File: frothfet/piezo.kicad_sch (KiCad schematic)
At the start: 3 parts, among them Q19 AO3400A

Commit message: piezo resistor
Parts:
- added R102: 100k, Resistor_SMD:R_0603_1608Metric, symbol Device:R_Small_US
- R90: value 1k -> 100R
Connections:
- net GNDD: now also R102.2
- net at Q19.1 (G), R90.1: now also R102.1
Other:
- moved on the sheet: R90
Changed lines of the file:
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@@
 		)
+	)
+	(junction
+		(at 134.62 109.22)
+		(diameter 0)
+		(color 0 0 0 0)
+	)
+	(junction
+		(at 124.46 100.33)
+		(diameter 0)
+		(color 0 0 0 0)
 	)
 	(wire
@@
 	(wire
 		(pts
-			(xy 123.19 100.33) (xy 127 100.33)
-		)
-		(stroke
-			(width 0)
-			(type default)
-		)
-	)
-	(wire
-		(pts
-			(xy 114.3 100.33) (xy 118.11 100.33)
+			(xy 134.62 109.22) (xy 124.46 109.22)
+		)
+		(stroke
+			(width 0)
+			(type default)
+		)
+	)
+	(wire
+		(pts
+			(xy 121.92 100.33) (xy 124.46 100.33)
+		)
+		(stroke
+			(width 0)
+			(type default)
+		)
+	)
+	(wire
+		(pts
+			(xy 124.46 109.22) (xy 124.46 107.95)
+		)
+		(stroke
+			(width 0)
+			(type default)
+		)
+	)
+	(wire
+		(pts
+			(xy 113.03 100.33) (xy 116.84 100.33)
+		)
+		(stroke
+			(width 0)
+			(type default)
+		)
+	)
+	(wire
+		(pts
+			(xy 124.46 100.33) (xy 127 100.33)
 		)
 		(stroke
@@
 		(pts
 			(xy 134.62 72.39) (xy 134.62 82.55)
+		)
+		(stroke
+			(width 0)
+			(type default)
+		)
+	)
+	(wire
+		(pts
+			(xy 124.46 100.33) (xy 124.46 102.87)
 		)
 		(stroke
@@
 	(hierarchical_label "PIEZO"
 		(shape input)
-		(at 114.3 100.33 180)
+		(at 113.03 100.33 180)
 		(effects
 			(font
@@
 	(symbol
 		(lib_id "Device:R_Small_US")
-		(at 120.65 100.33 270)
+		(at 124.46 105.41 0)
+		(unit 1)
+		(exclude_from_sim no)
+		(in_bom yes)
+		(on_board yes)
+		(dnp no)
+		(fields_autoplaced yes)
+		(property "Reference" "R102"
+			(at 127 104.1399 0)
+			(effects
+				(font
+					(size 1.27 1.27)
+				)
+				(justify left)
+			)
+		)
+		(property "Value" "100k"
+			(at 127 106.6799 0)
+			(effects
+				(font
+					(size 1.27 1.27)
+				)
+				(justify left)
+			)
+		)
+		(property "Footprint" "Resistor_SMD:R_0603_1608Metric"
+			(at 124.46 105.41 0)
+			(effects
+				(font
+					(size 1.27 1.27)
+				)
+				(hide yes)
+			)
+		)
+		(property "Datasheet" "~"
+			(at 124.46 105.41 0)
+			(effects
+				(font
+					(size 1.27 1.27)
+				)
+				(hide yes)
+			)
+		)
+		(property "Description" ""
+			(at 124.46 105.41 0)
+			(effects
+				(font
+					(size 1.27 1.27)
+				)
+				(hide yes)
+			)
+		)
+		(pin "1"
+		)
+		(pin "2"
+		)
+		(instances
+			(project "frothfet"
+				(path "/c83c6236-96e9-46ad-9d7a-9e2efa4a7966/13bd1484-e1d0-414c-b70b-256f3904dbbc"
+					(reference "R102")
+					(unit 1)
+				)
+			)
+		)
+	)
+	(symbol
+		(lib_id "Device:R_Small_US")
+		(at 119.38 100.33 270)
 		(unit 1)
 		(exclude_from_sim no)
@@
 		(fields_autoplaced yes)
 		(property "Reference" "R90"
-			(at 120.65 93.98 90)
-			(effects
-				(font
-					(size 1.27 1.27)
-				)
-			)
-		)
-		(property "Value" "1k"
-			(at 120.65 96.52 90)
+			(at 119.38 93.98 90)
+			(effects
+				(font
+					(size 1.27 1.27)
+				)
+			)
+		)
+		(property "Value" "100R"
+			(at 119.38 96.52 90)
 			(effects
 				(font
@@
 		)
 		(property "Footprint" "Resistor_SMD:R_0603_1608Metric"
-			(at 120.65 100.33 0)
+			(at 119.38 100.33 0)
 			(effects
 				(font
@@
 		)
 		(property "Datasheet" "~"
-			(at 120.65 100.33 0)
+			(at 119.38 100.33 0)
 			(effects
 				(font
@@
 		)
 		(property "Description" ""
-			(at 120.65 100.33 0)
-			(effects
-				(font
-					(size 1.27 1.27)
-				)
-				(hide yes)
-			)
-		)
-		(property "LCSC" ""
-			(at 120.65 100.33 0)
-			(effects
-				(font
-					(size 1.27 1.27)
-				)
-				(hide yes)
-			)
-		)
-		(property "ALT" ""
-			(at 120.65 100.33 0)
-			(effects
-				(font
+			(at 119.38 100.33 0)
+			(effects
+				(font

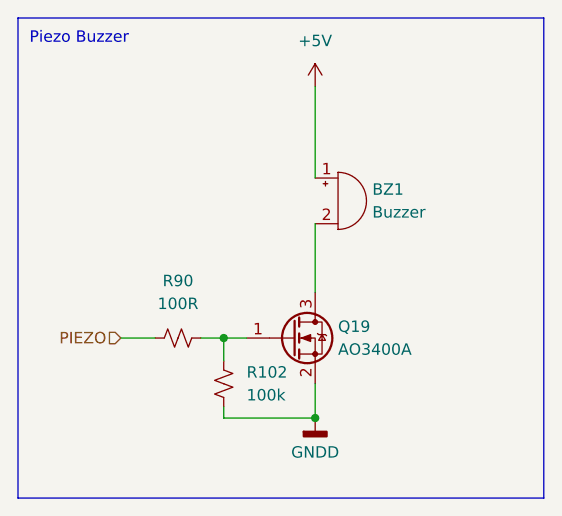
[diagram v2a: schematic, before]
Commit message: silkscreen done, erc+drc passing
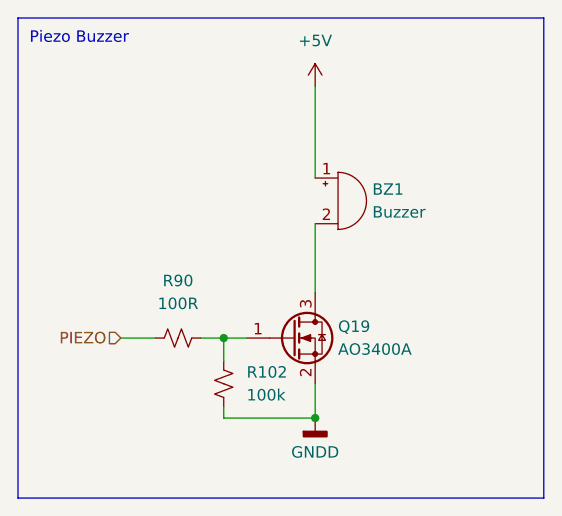
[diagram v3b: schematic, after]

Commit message: bom and placement all check out.  ready for production!
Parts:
- BZ1: Rotation Offset (none) -> 90
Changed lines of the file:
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@@
+			)
+		)
+		(property "Rotation Offset" "90"
+			(at 137.16 85.09 0)
+			(effects
+				(font
+					(size 1.27 1.27)
+				)
+				(hide yes)
 			)
 		)

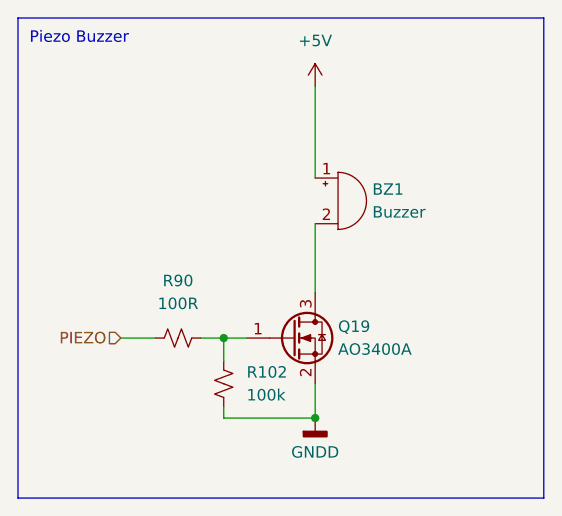
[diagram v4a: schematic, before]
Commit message: pulled in updated esp32-s3 schematic
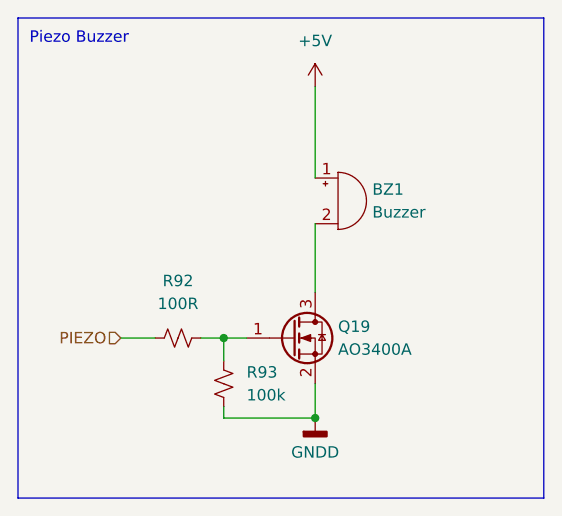
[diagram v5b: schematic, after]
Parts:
- renumbered R90 to R92, R102 to R93
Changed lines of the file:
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@@
 		(dnp no)
 		(fields_autoplaced yes)
-		(property "Reference" "R102"
+		(property "Reference" "R93"
 			(at 127 104.1399 0)
 			(effects
@@
 			(project "frothfet"
 				(path "/c83c6236-96e9-46ad-9d7a-9e2efa4a7966/13bd1484-e1d0-414c-b70b-256f3904dbbc"
-					(reference "R102")
+					(reference "R93")
 					(unit 1)
 				)
@@
 		(dnp no)
 		(fields_autoplaced yes)
-		(property "Reference" "R90"
+		(property "Reference" "R92"
 			(at 119.38 93.98 90)
 			(effects
@@
 			(project "frothfet"
 				(path "/c83c6236-96e9-46ad-9d7a-9e2efa4a7966/13bd1484-e1d0-414c-b70b-256f3904dbbc"
-					(reference "R90")
+					(reference "R92")
 					(unit 1)
 				)
@@
 		(dnp no)
 		(fields_autoplaced yes)
-		(property "Reference" "#PWR0122"
+		(property "Reference" "#PWR0119"
 			(at 134.62 76.2 0)
 			(effects
@@
 			(project "frothfet"
 				(path "/c83c6236-96e9-46ad-9d7a-9e2efa4a7966/13bd1484-e1d0-414c-b70b-256f3904dbbc"
-					(reference "#PWR0122")
+					(reference "#PWR0119")
 					(unit 1)
 				)
@@
 		(dnp no)
 		(fields_autoplaced yes)
-		(property "Reference" "#PWR0123"
+		(property "Reference" "#PWR0120"
 			(at 134.62 115.57 0)
 			(effects
@@
 			(project "frothfet"
 				(path "/c83c6236-96e9-46ad-9d7a-9e2efa4a7966/13bd1484-e1d0-414c-b70b-256f3904dbbc"
-					(reference "#PWR0123")
-					(unit 1)
-				)
+					(reference "#PWR0120")
+					(unit 1)
+				)

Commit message: wired the i2c addresses.
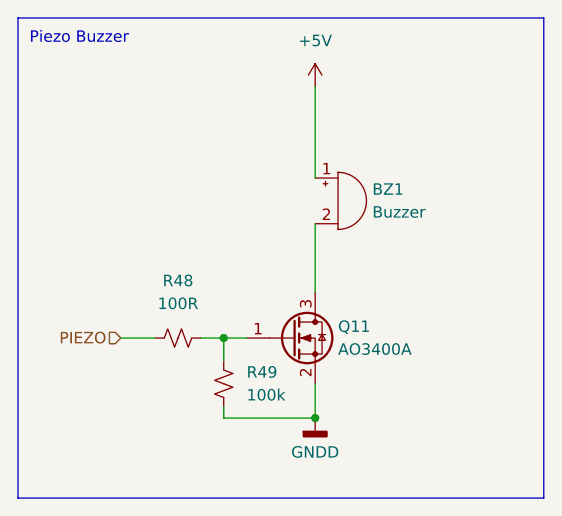
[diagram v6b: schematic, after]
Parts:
- renumbered Q19 to Q11, R92 to R48, R93 to R49
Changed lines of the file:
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@@
 		(dnp no)
 		(fields_autoplaced yes)
-		(property "Reference" "R93"
+		(property "Reference" "R49"
 			(at 127 104.1399 0)
 			(effects
@@
 			(project "frothfet"
 				(path "/c83c6236-96e9-46ad-9d7a-9e2efa4a7966/13bd1484-e1d0-414c-b70b-256f3904dbbc"
-					(reference "R93")
+					(reference "R49")
 					(unit 1)
 				)
@@
 		(dnp no)
 		(fields_autoplaced yes)
-		(property "Reference" "R92"
+		(property "Reference" "R48"
 			(at 119.38 93.98 90)
 			(effects
@@
 			(project "frothfet"
 				(path "/c83c6236-96e9-46ad-9d7a-9e2efa4a7966/13bd1484-e1d0-414c-b70b-256f3904dbbc"
-					(reference "R92")
+					(reference "R48")
 					(unit 1)
 				)
@@
 		(on_board yes)
 		(dnp no)
-		(property "Reference" "Q19"
+		(property "Reference" "Q11"
 			(at 137.16 99.06 0)
 			(effects
@@
 			(project "frothfet"
 				(path "/c83c6236-96e9-46ad-9d7a-9e2efa4a7966/13bd1484-e1d0-414c-b70b-256f3904dbbc"
-					(reference "Q19")
+					(reference "Q11")
 					(unit 1)
 				)
@@
 		(dnp no)
 		(fields_autoplaced yes)
-		(property "Reference" "#PWR0119"
+		(property "Reference" "#PWR096"
 			(at 134.62 76.2 0)
 			(effects
@@
 			(project "frothfet"
 				(path "/c83c6236-96e9-46ad-9d7a-9e2efa4a7966/13bd1484-e1d0-414c-b70b-256f3904dbbc"
-					(reference "#PWR0119")
+					(reference "#PWR096")
 					(unit 1)
 				)
@@
 		(dnp no)
 		(fields_autoplaced yes)
-		(property "Reference" "#PWR0120"
+		(property "Reference" "#PWR097"
 			(at 134.62 115.57 0)
 			(effects
@@
 			(project "frothfet"
 				(path "/c83c6236-96e9-46ad-9d7a-9e2efa4a7966/13bd1484-e1d0-414c-b70b-256f3904dbbc"
-					(reference "#PWR0120")
-					(unit 1)
-				)
+					(reference "#PWR097")
+					(unit 1)
+				)

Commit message: added the buffer circuit
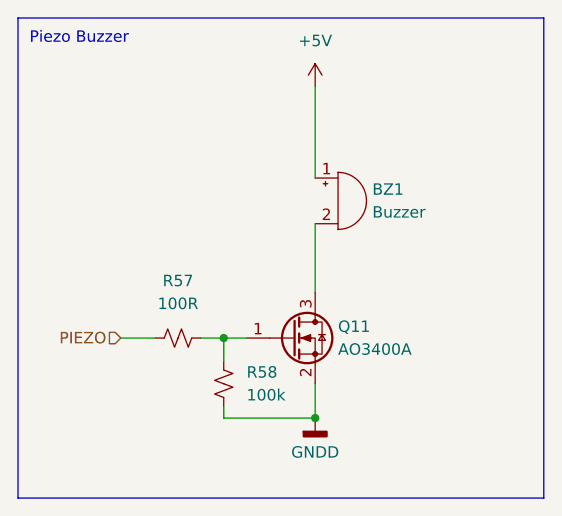
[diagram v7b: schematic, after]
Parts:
- renumbered R48 to R57, R49 to R58
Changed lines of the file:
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@@
 		(dnp no)
 		(fields_autoplaced yes)
-		(property "Reference" "R49"
+		(property "Reference" "R58"
 			(at 127 104.1399 0)
 			(effects
@@
 			(project "frothfet"
 				(path "/c83c6236-96e9-46ad-9d7a-9e2efa4a7966/13bd1484-e1d0-414c-b70b-256f3904dbbc"
-					(reference "R49")
+					(reference "R58")
 					(unit 1)
 				)
@@
 		(dnp no)
 		(fields_autoplaced yes)
-		(property "Reference" "R48"
+		(property "Reference" "R57"
 			(at 119.38 93.98 90)
 			(effects
@@
 			(project "frothfet"
 				(path "/c83c6236-96e9-46ad-9d7a-9e2efa4a7966/13bd1484-e1d0-414c-b70b-256f3904dbbc"
-					(reference "R48")
+					(reference "R57")
 					(unit 1)
 				)
@@
 		(dnp no)
 		(fields_autoplaced yes)
-		(property "Reference" "#PWR096"
+		(property "Reference" "#PWR0135"
 			(at 134.62 76.2 0)
 			(effects
@@
 			(project "frothfet"
 				(path "/c83c6236-96e9-46ad-9d7a-9e2efa4a7966/13bd1484-e1d0-414c-b70b-256f3904dbbc"
-					(reference "#PWR096")
+					(reference "#PWR0135")
 					(unit 1)
 				)
@@
 		(dnp no)
 		(fields_autoplaced yes)
-		(property "Reference" "#PWR097"
+		(property "Reference" "#PWR0136"
 			(at 134.62 115.57 0)
 			(effects
@@
 			(project "frothfet"
 				(path "/c83c6236-96e9-46ad-9d7a-9e2efa4a7966/13bd1484-e1d0-414c-b70b-256f3904dbbc"
-					(reference "#PWR097")
-					(unit 1)
-				)
+					(reference "#PWR0136")
+					(unit 1)
+				)

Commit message: changed to a single ground
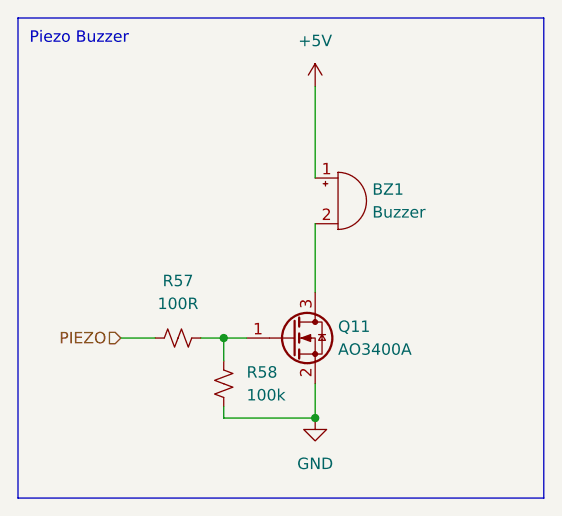
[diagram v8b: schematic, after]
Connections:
- net GNDD renamed GND
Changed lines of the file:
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@@
 	)
 	(symbol
-		(lib_id "power:GNDD")
+		(lib_id "power:GND")
 		(at 134.62 109.22 0)
 		(unit 1)
@@
 		(dnp no)
 		(fields_autoplaced yes)
-		(property "Reference" "#PWR0136"
+		(property "Reference" "#PWR136"
 			(at 134.62 115.57 0)
 			(effects
@@
 			)
 		)
-		(property "Value" "GNDD"
-			(at 134.62 113.03 0)
+		(property "Value" "GND"
+			(at 134.62 114.3 0)
 			(effects
 				(font
@@
 			)
 		)
-		(property "Description" "Power symbol creates a global label with name \"GNDD\" , digital ground"
+		(property "Description" "Power symbol creates a global label with name \"GND\" , ground"
 			(at 134.62 109.22 0)
 			(effects
@@
 			(project "frothfet"
 				(path "/c83c6236-96e9-46ad-9d7a-9e2efa4a7966/13bd1484-e1d0-414c-b70b-256f3904dbbc"
-					(reference "#PWR0136")
+					(reference "#PWR136")
 					(unit 1)
 				)
